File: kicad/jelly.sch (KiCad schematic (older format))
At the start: 41 parts, among them M1 PAGER_MOTOR, M2 PAGER_MOTOR, P1 CONN_01X01, P10 CONN_01X01, P11 CONN_01X01, P12 CONN_01X01, P13 CONN_01X01, P14 CONN_01X01, P15 CONN_01X01, P2 CONN_01X01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

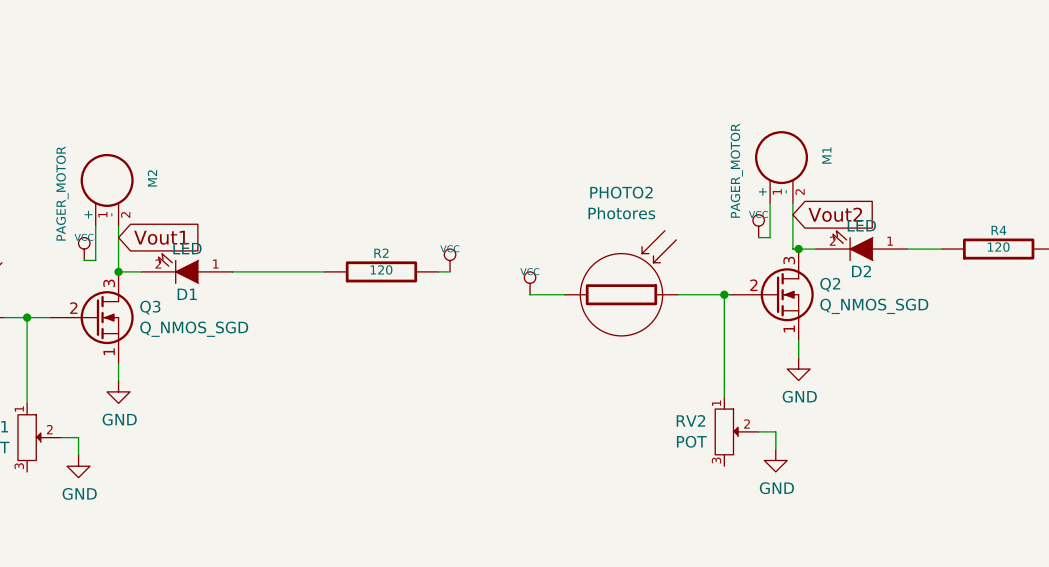
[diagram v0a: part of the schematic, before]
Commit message: Rename leds from D to LED
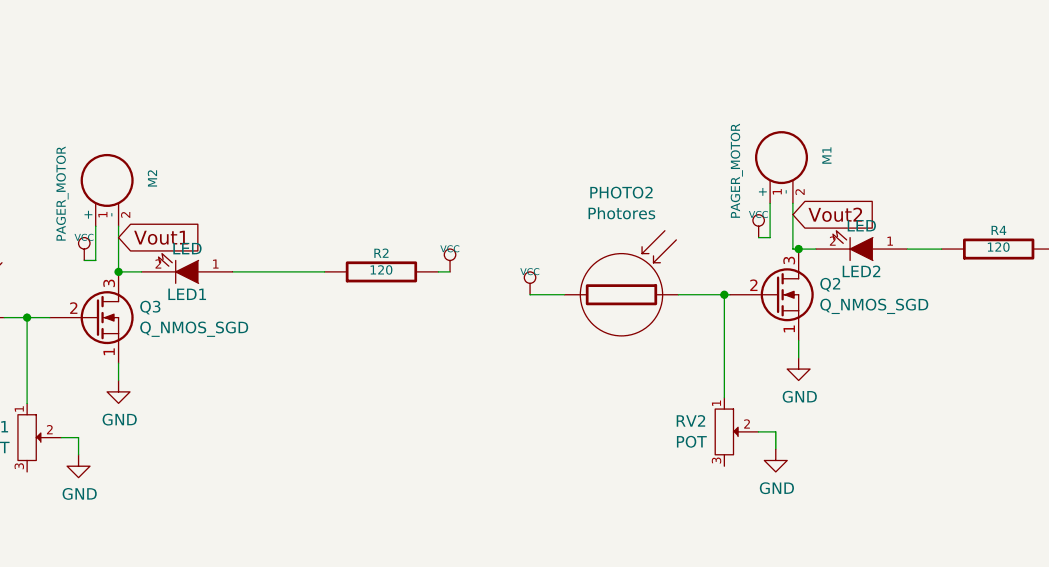
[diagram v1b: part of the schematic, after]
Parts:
- renumbered D1 to LED1, D2 to LED2
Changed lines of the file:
@@
 $EndComp
 $Comp
-L LED-RESCUE-bristle_bot D2
+L LED-RESCUE-bristle_bot LED2
 U 1 1 57C0D39F
 P 8600 2600
-F 0 "D2" H 8600 2700 50  0000 C CNN
+F 0 "LED2" H 8600 2700 50  0000 C CNN
 F 1 "LED" H 8600 2500 50  0000 C CNN
 F 2 "KiCad/LEDs.pretty:LED-5MM" H 8600 2600 29  0001 C CNN
@@
 $EndComp
 $Comp
-L LED-RESCUE-bristle_bot D1
+L LED-RESCUE-bristle_bot LED1
 U 1 1 57C0D3A3
 P 5650 2700
-F 0 "D1" H 5650 2800 50  0000 C CNN
+F 0 "LED1" H 5650 2800 50  0000 C CNN
 F 1 "LED" H 5650 2600 50  0000 C CNN
 F 2 "KiCad/LEDs.pretty:LED-5MM" H 5650 2700 60  0001 C CNN

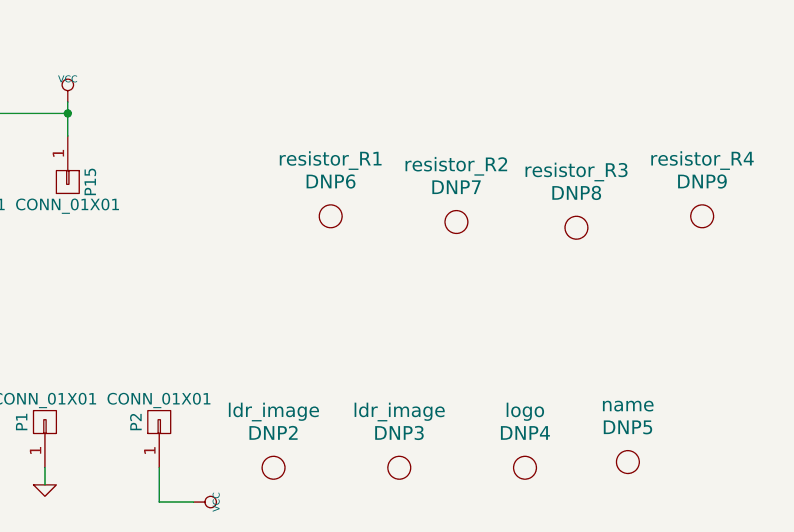
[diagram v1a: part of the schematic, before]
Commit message: Add page motor silkscreen image
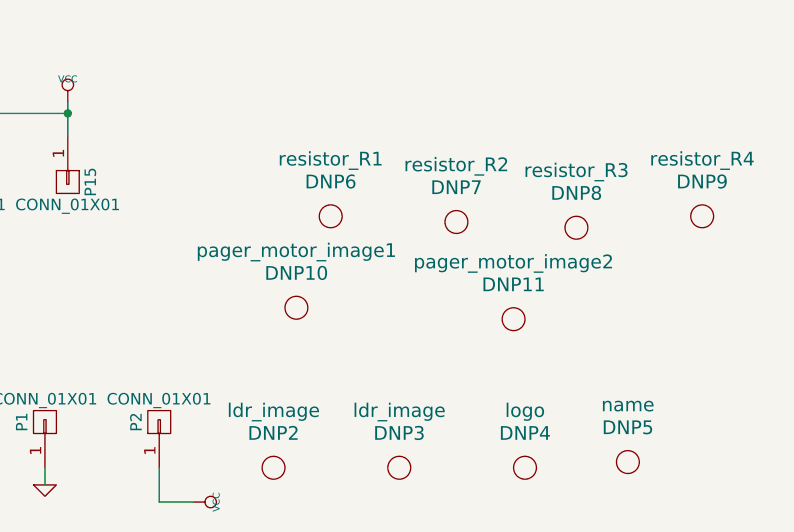
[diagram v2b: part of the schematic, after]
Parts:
- added DNP10: pager_motor_image1, custom:page_motor_image, symbol placeholder
- added DNP11: pager_motor_image2, custom:page_motor_image_flipped, symbol placeholder
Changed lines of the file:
@@
+	1    0    0    -1
+$EndComp
+$Comp
+L placeholder DNP10
+U 1 1 5802A5F3
+P 8900 5500
+F 0 "DNP10" H 8900 5650 60  0000 C CNN
+F 1 "pager_motor_image1" H 8900 5750 60  0000 C CNN
+F 2 "custom:page_motor_image" H 8900 5650 60  0001 C CNN
+F 3 "" H 8900 5650 60  0001 C CNN
+	1    8900 5500
+	1    0    0    -1
+$EndComp
+$Comp
+L placeholder DNP11
+U 1 1 5802A756
+P 9850 5550
+F 0 "DNP11" H 9850 5700 60  0000 C CNN
+F 1 "pager_motor_image2" H 9850 5800 60  0000 C CNN
+F 2 "custom:page_motor_image_flipped" H 9850 5700 60  0001 C CNN
+F 3 "" H 9850 5700 60  0001 C CNN
+	1    9850 5550
 	1    0    0    -1
 $EndComp

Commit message: Add plus and minus labels
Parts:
- added DNP12: plus1, custom:plus, symbol placeholder
- added DNP13: minus1, custom:minus, symbol placeholder
- BT1, SW1: footprint KiCad/Pin_Headers.pretty:Pin_Header_Straight_1x02 -> custom:Pin_Header_Straight_1x02
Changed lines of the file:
@@
 F 0 "BT1" H 1325 1925 50  0000 C CNN
 F 1 "BATTERY" H 1325 1535 50  0000 C CNN
-F 2 "KiCad/Pin_Headers.pretty:Pin_Header_Straight_1x02" H 1325 1725 29  0001 C CNN
+F 2 "custom:Pin_Header_Straight_1x02" H 1325 1725 29  0001 C CNN
 F 3 "~" H 1325 1725 60  0000 C CNN
 	1    1325 1725
@@
 F 0 "SW1" V 2271 1922 50  0000 R CNN
 F 1 "SPST" V 2180 1922 50  0000 R CNN
-F 2 "KiCad/Pin_Headers.pretty:Pin_Header_Straight_1x02" H 2225 2000 50  0001 C CNN
+F 2 "custom:Pin_Header_Straight_1x02" H 2225 2000 50  0001 C CNN
 F 3 "" H 2225 2000 50  0000 C CNN
 	1    2225 2000
@@
 	1    0    0    -1
 $EndComp
+$Comp
+L placeholder DNP12
+U 1 1 5802B04C
+P 10600 5625
+F 0 "DNP12" H 10600 5775 60  0000 C CNN
+F 1 "plus1" H 10600 5875 60  0000 C CNN
+F 2 "custom:plus" H 10600 5775 60  0001 C CNN
+F 3 "" H 10600 5775 60  0001 C CNN
+	1    10600 5625
+	1    0    0    -1
+$EndComp
+$Comp
+L placeholder DNP13
+U 1 1 5802B75C
+P 10900 5700
+F 0 "DNP13" H 10900 5850 60  0000 C CNN
+F 1 "minus1" H 10900 5950 60  0000 C CNN
+F 2 "custom:minus" H 10900 5850 60  0001 C CNN
+F 3 "" H 10900 5850 60  0001 C CNN
+	1    10900 5700
+	1    0    0    -1
+$EndComp

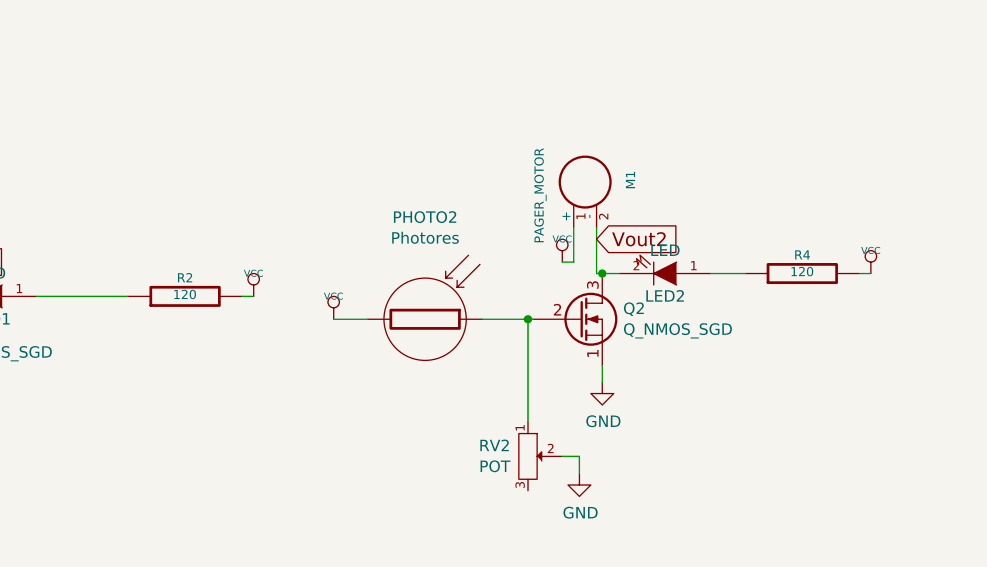
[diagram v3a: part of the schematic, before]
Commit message: Delete traces and make things more symmetrical
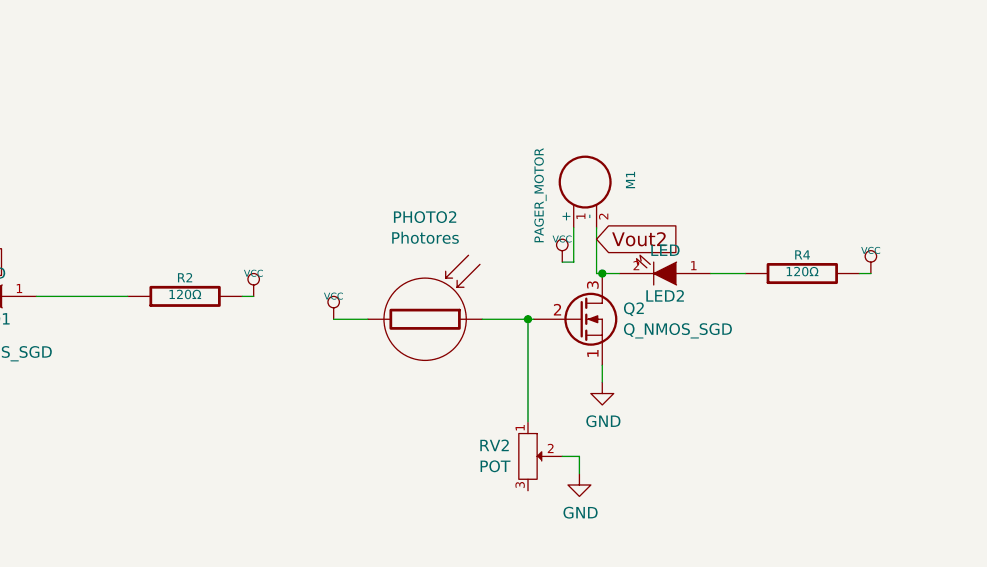
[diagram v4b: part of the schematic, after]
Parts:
- R2, R4: value 120 -> 120Ω
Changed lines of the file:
@@
 P 9200 2600
 F 0 "R4" V 9280 2600 40  0000 C CNN
-F 1 "120" V 9207 2601 40  0000 C CNN
+F 1 "120Ω" V 9207 2601 40  0000 C CNN
 F 2 "custom:R3-5" V 9130 2600 30  0001 C CNN
 F 3 "~" H 9200 2600 30  0000 C CNN
@@
 P 6500 2700
 F 0 "R2" V 6580 2700 40  0000 C CNN
-F 1 "120" V 6507 2701 40  0000 C CNN
+F 1 "120Ω" V 6507 2701 40  0000 C CNN
 F 2 "custom:R3-5" V 6430 2700 30  0001 C CNN
 F 3 "~" H 6500 2700 30  0000 C CNN

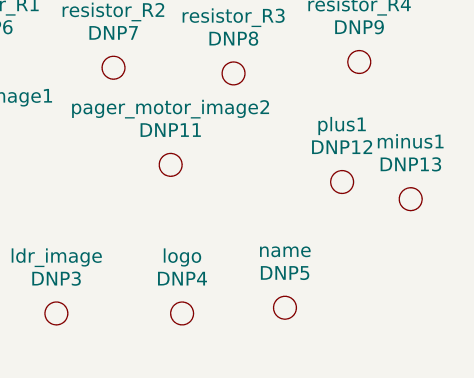
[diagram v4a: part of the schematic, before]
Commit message: Add mercury switch drawing
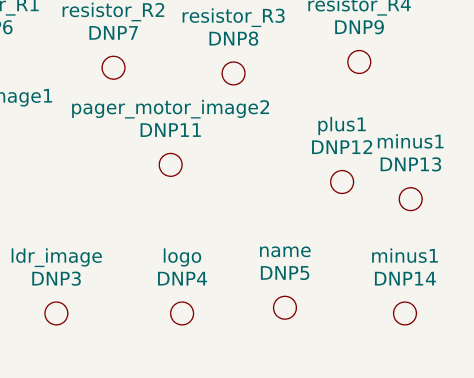
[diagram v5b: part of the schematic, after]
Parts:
- added DNP14: minus1, custom:mercury_switch, symbol placeholder
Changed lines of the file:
@@
 $EndComp
 $Comp
-L GND-RESCUE-bristle_bot #PWR01
+L GND-RESCUE-bristle_bot #PWR2
 U 1 1 57C0D38E
 P 1325 3225
-F 0 "#PWR01" H 1325 3225 30  0001 C CNN
+F 0 "#PWR2" H 1325 3225 30  0001 C CNN
 F 1 "GND" H 1325 3155 30  0001 C CNN
 F 2 "" H 1325 3225 60  0000 C CNN
@@
 $EndComp
 $Comp
-L VCC #PWR02
+L VCC #PWR1
 U 1 1 57C0D391
 P 1325 1275
-F 0 "#PWR02" H 1325 1375 30  0001 C CNN
+F 0 "#PWR1" H 1325 1375 30  0001 C CNN
 F 1 "VCC" H 1325 1375 30  0000 C CNN
 F 2 "" H 1325 1275 60  0001 C CNN
@@
 $EndComp
 $Comp
-L VCC #PWR03
+L VCC #PWR5
 U 1 1 57C0D393
 P 4200 2900
-F 0 "#PWR03" H 4200 3000 30  0001 C CNN
+F 0 "#PWR5" H 4200 3000 30  0001 C CNN
 F 1 "VCC" H 4200 3000 30  0000 C CNN
 F 2 "" H 4200 2900 60  0001 C CNN
@@
 $EndComp
 $Comp
-L VCC #PWR04
+L VCC #PWR8
 U 1 1 57C0D394
 P 5200 2650
-F 0 "#PWR04" H 5200 2750 30  0001 C CNN
+F 0 "#PWR8" H 5200 2750 30  0001 C CNN
 F 1 "VCC" H 5200 2750 30  0000 C CNN
 F 2 "" H 5200 2650 60  0001 C CNN
@@
 $EndComp
 $Comp
-L VCC #PWR05
+L VCC #PWR14
 U 1 1 57C0D397
 P 8150 2550
-F 0 "#PWR05" H 8150 2650 30  0001 C CNN
+F 0 "#PWR14" H 8150 2650 30  0001 C CNN
 F 1 "VCC" H 8150 2650 30  0000 C CNN
 F 2 "" H 8150 2550 60  0001 C CNN
@@
 $EndComp
 $Comp
-L VCC #PWR06
+L VCC #PWR11
 U 1 1 57C0D39B
 P 7150 2800
-F 0 "#PWR06" H 7150 2900 30  0001 C CNN
+F 0 "#PWR11" H 7150 2900 30  0001 C CNN
 F 1 "VCC" H 7150 2900 30  0000 C CNN
 F 2 "" H 7150 2800 60  0001 C CNN
@@
 $EndComp
 $Comp
-L VCC #PWR07
+L VCC #PWR18
 U 1 1 57C0D3A1
 P 9500 2600
-F 0 "#PWR07" H 9500 2700 30  0001 C CNN
+F 0 "#PWR18" H 9500 2700 30  0001 C CNN
 F 1 "VCC" H 9500 2700 30  0000 C CNN
 F 2 "" H 9500 2600 60  0001 C CNN
@@
 $EndComp
 $Comp
-L VCC #PWR08
+L VCC #PWR10
 U 1 1 57C0D3A4
 P 6800 2700
-F 0 "#PWR08" H 6800 2800 30  0001 C CNN
+F 0 "#PWR10" H 6800 2800 30  0001 C CNN
 F 1 "VCC" H 6800 2800 30  0000 C CNN
 F 2 "" H 6800 2700 60  0001 C CNN
@@
 $EndComp
 $Comp
-L VCC #PWR09
+L VCC #PWR3
 U 1 1 57C0D3B0
 P 1450 4350
-F 0 "#PWR09" H 1450 4450 30  0001 C CNN
+F 0 "#PWR3" H 1450 4450 30  0001 C CNN
 F 1 "VCC" H 1450 4450 30  0000 C CNN
 F 2 "" H 1450 4350 60  0001 C CNN
@@
 $EndComp
 $Comp
-L VCC #PWR010
+L VCC #PWR13
 U 1 1 57C309E3
 P 7900 4600
-F 0 "#PWR010" H 7900 4700 30  0001 C CNN
+F 0 "#PWR13" H 7900 4700 30  0001 C CNN
 F 1 "VCC" H 7900 4700 30  0000 C CNN
 F 2 "" H 7900 4600 60  0001 C CNN
@@
 Vout2
 $Comp
-L GND-RESCUE-bristle_bot #PWR011
+L GND-RESCUE-bristle_bot #PWR6
 U 1 1 57C36163
 P 4600 4550
-F 0 "#PWR011" H 4600 4550 30  0001 C CNN
+F 0 "#PWR6" H 4600 4550 30  0001 C CNN
 F 1 "GND" H 4600 4480 30  0001 C CNN
 F 2 "" H 4600 4550 60  0001 C CNN
@@
 $EndComp
 $Comp
-L VCC #PWR012
+L VCC #PWR17
 U 1 1 57C3486C
 P 8450 6350
-F 0 "#PWR012" H 8450 6450 30  0001 C CNN
+F 0 "#PWR17" H 8450 6450 30  0001 C CNN
 F 1 "VCC" H 8450 6450 30  0000 C CNN
 F 2 "" H 8450 6350 60  0001 C CNN
@@
 $EndComp
 $Comp
-L GND #PWR013
+L GND #PWR9
 U 1 1 57EC11E5
 P 5350 3175
-F 0 "#PWR013" H 5350 2925 50  0001 C CNN
+F 0 "#PWR9" H 5350 2925 50  0001 C CNN
 F 1 "GND" H 5355 3002 50  0000 C CNN
 F 2 "" H 5350 3175 50  0000 C CNN
@@
 $EndComp
 $Comp
-L GND #PWR014
+L GND #PWR16
 U 1 1 57EC1326
 P 8325 3075
-F 0 "#PWR014" H 8325 2825 50  0001 C CNN
+F 0 "#PWR16" H 8325 2825 50  0001 C CNN
 F 1 "GND" H 8330 2902 50  0000 C CNN
 F 2 "" H 8325 3075 50  0000 C CNN
@@
 $EndComp
 $Comp
-L GND #PWR015
+L GND #PWR7
 U 1 1 57EC1A42
 P 5175 3500
-F 0 "#PWR015" H 5175 3250 50  0001 C CNN
+F 0 "#PWR7" H 5175 3250 50  0001 C CNN
 F 1 "GND" H 5180 3327 50  0000 C CNN
 F 2 "" H 5175 3500 50  0000 C CNN
@@
 $EndComp
 $Comp
-L GND #PWR016
+L GND #PWR15
 U 1 1 57EC1E47
 P 8225 3475
-F 0 "#PWR016" H 8225 3225 50  0001 C CNN
+F 0 "#PWR15" H 8225 3225 50  0001 C CNN
 F 1 "GND" H 8230 3302 50  0000 C CNN
 F 2 "" H 8225 3475 50  0000 C CNN
@@
 Connection ~ 2225 3000
 $Comp
-L GND-RESCUE-bristle_bot #PWR017
+L GND-RESCUE-bristle_bot #PWR4
 U 1 1 57EC6243
 P 2225 3575
-F 0 "#PWR017" H 2225 3575 30  0001 C CNN
+F 0 "#PWR4" H 2225 3575 30  0001 C CNN
 F 1 "GND" H 2225 3505 30  0001 C CNN
 F 2 "" H 2225 3575 60  0000 C CNN
@@
 	1325 2700 1325 2025
 $Comp
-L GND-RESCUE-bristle_bot #PWR018
+L GND-RESCUE-bristle_bot #PWR12
 U 1 1 57F92FC8
 P 7800 6275
-F 0 "#PWR018" H 7800 6275 30  0001 C CNN
+F 0 "#PWR12" H 7800 6275 30  0001 C CNN
 F 1 "GND" H 7800 6205 30  0001 C CNN
 F 2 "" H 7800 6275 60  0000 C CNN
@@
 	1    0    0    -1
 $EndComp
+$Comp
+L placeholder DNP14
+U 1 1 5802C4A0
+P 10875 6200
+F 0 "DNP14" H 10875 6350 60  0000 C CNN
+F 1 "minus1" H 10875 6450 60  0000 C CNN
+F 2 "custom:mercury_switch" H 10875 6350 60  0001 C CNN
+F 3 "" H 10875 6350 60  0001 C CNN
+	1    10875 6200
+	1    0    0    -1
+$EndComp

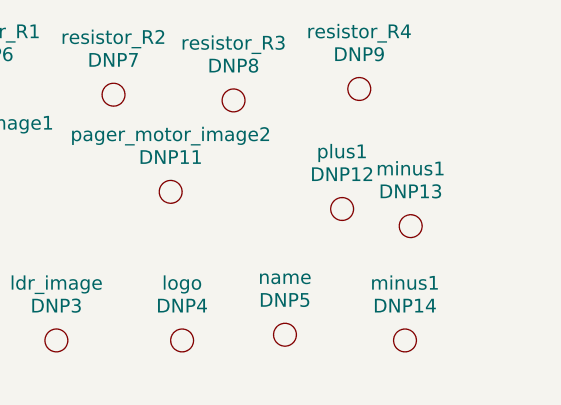
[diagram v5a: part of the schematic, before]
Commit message: Make sure footprints and schematic are in sync
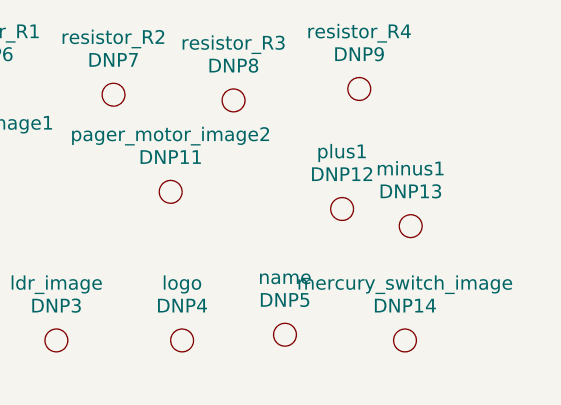
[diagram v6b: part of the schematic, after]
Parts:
- DNP14: value minus1 -> mercury_switch_image
- SW1: footprint custom:Pin_Header_Straight_1x02 -> custom:MERCURY_SWITCH_HEADER
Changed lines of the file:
@@
 $EndComp
 $Comp
-L GND-RESCUE-bristle_bot #PWR2
+L GND-RESCUE-bristle_bot #PWR01
 U 1 1 57C0D38E
 P 1325 3225
-F 0 "#PWR2" H 1325 3225 30  0001 C CNN
+F 0 "#PWR01" H 1325 3225 30  0001 C CNN
 F 1 "GND" H 1325 3155 30  0001 C CNN
 F 2 "" H 1325 3225 60  0000 C CNN
@@
 $EndComp
 $Comp
-L VCC #PWR1
+L VCC #PWR02
 U 1 1 57C0D391
 P 1325 1275
-F 0 "#PWR1" H 1325 1375 30  0001 C CNN
+F 0 "#PWR02" H 1325 1375 30  0001 C CNN
 F 1 "VCC" H 1325 1375 30  0000 C CNN
 F 2 "" H 1325 1275 60  0001 C CNN
@@
 $EndComp
 $Comp
-L VCC #PWR5
+L VCC #PWR03
 U 1 1 57C0D393
 P 4200 2900
-F 0 "#PWR5" H 4200 3000 30  0001 C CNN
+F 0 "#PWR03" H 4200 3000 30  0001 C CNN
 F 1 "VCC" H 4200 3000 30  0000 C CNN
 F 2 "" H 4200 2900 60  0001 C CNN
@@
 $EndComp
 $Comp
-L VCC #PWR8
+L VCC #PWR04
 U 1 1 57C0D394
 P 5200 2650
-F 0 "#PWR8" H 5200 2750 30  0001 C CNN
+F 0 "#PWR04" H 5200 2750 30  0001 C CNN
 F 1 "VCC" H 5200 2750 30  0000 C CNN
 F 2 "" H 5200 2650 60  0001 C CNN
@@
 $EndComp
 $Comp
-L VCC #PWR14
+L VCC #PWR05
 U 1 1 57C0D397
 P 8150 2550
-F 0 "#PWR14" H 8150 2650 30  0001 C CNN
+F 0 "#PWR05" H 8150 2650 30  0001 C CNN
 F 1 "VCC" H 8150 2650 30  0000 C CNN
 F 2 "" H 8150 2550 60  0001 C CNN
@@
 $EndComp
 $Comp
-L VCC #PWR11
+L VCC #PWR06
 U 1 1 57C0D39B
 P 7150 2800
-F 0 "#PWR11" H 7150 2900 30  0001 C CNN
+F 0 "#PWR06" H 7150 2900 30  0001 C CNN
 F 1 "VCC" H 7150 2900 30  0000 C CNN
 F 2 "" H 7150 2800 60  0001 C CNN
@@
 $EndComp
 $Comp
-L VCC #PWR18
+L VCC #PWR07
 U 1 1 57C0D3A1
 P 9500 2600
-F 0 "#PWR18" H 9500 2700 30  0001 C CNN
+F 0 "#PWR07" H 9500 2700 30  0001 C CNN
 F 1 "VCC" H 9500 2700 30  0000 C CNN
 F 2 "" H 9500 2600 60  0001 C CNN
@@
 $EndComp
 $Comp
-L VCC #PWR10
+L VCC #PWR08
 U 1 1 57C0D3A4
 P 6800 2700
-F 0 "#PWR10" H 6800 2800 30  0001 C CNN
+F 0 "#PWR08" H 6800 2800 30  0001 C CNN
 F 1 "VCC" H 6800 2800 30  0000 C CNN
 F 2 "" H 6800 2700 60  0001 C CNN
@@
 $EndComp
 $Comp
-L VCC #PWR3
+L VCC #PWR09
 U 1 1 57C0D3B0
 P 1450 4350
-F 0 "#PWR3" H 1450 4450 30  0001 C CNN
+F 0 "#PWR09" H 1450 4450 30  0001 C CNN
 F 1 "VCC" H 1450 4450 30  0000 C CNN
 F 2 "" H 1450 4350 60  0001 C CNN
@@
 $EndComp
 $Comp
-L VCC #PWR13
+L VCC #PWR010
 U 1 1 57C309E3
 P 7900 4600
-F 0 "#PWR13" H 7900 4700 30  0001 C CNN
+F 0 "#PWR010" H 7900 4700 30  0001 C CNN
 F 1 "VCC" H 7900 4700 30  0000 C CNN
 F 2 "" H 7900 4600 60  0001 C CNN
@@
 Vout2
 $Comp
-L GND-RESCUE-bristle_bot #PWR6
+L GND-RESCUE-bristle_bot #PWR011
 U 1 1 57C36163
 P 4600 4550
-F 0 "#PWR6" H 4600 4550 30  0001 C CNN
+F 0 "#PWR011" H 4600 4550 30  0001 C CNN
 F 1 "GND" H 4600 4480 30  0001 C CNN
 F 2 "" H 4600 4550 60  0001 C CNN
@@
 $EndComp
 $Comp
-L VCC #PWR17
+L VCC #PWR012
 U 1 1 57C3486C
 P 8450 6350
-F 0 "#PWR17" H 8450 6450 30  0001 C CNN
+F 0 "#PWR012" H 8450 6450 30  0001 C CNN
 F 1 "VCC" H 8450 6450 30  0000 C CNN
 F 2 "" H 8450 6350 60  0001 C CNN
@@
 $EndComp
 $Comp
-L GND #PWR9
+L GND #PWR013
 U 1 1 57EC11E5
 P 5350 3175
-F 0 "#PWR9" H 5350 2925 50  0001 C CNN
+F 0 "#PWR013" H 5350 2925 50  0001 C CNN
 F 1 "GND" H 5355 3002 50  0000 C CNN
 F 2 "" H 5350 3175 50  0000 C CNN
@@
 $EndComp
 $Comp
-L GND #PWR16
+L GND #PWR014
 U 1 1 57EC1326
 P 8325 3075
-F 0 "#PWR16" H 8325 2825 50  0001 C CNN
+F 0 "#PWR014" H 8325 2825 50  0001 C CNN
 F 1 "GND" H 8330 2902 50  0000 C CNN
 F 2 "" H 8325 3075 50  0000 C CNN
@@
 $EndComp
 $Comp
-L GND #PWR7
+L GND #PWR015
 U 1 1 57EC1A42
 P 5175 3500
-F 0 "#PWR7" H 5175 3250 50  0001 C CNN
+F 0 "#PWR015" H 5175 3250 50  0001 C CNN
 F 1 "GND" H 5180 3327 50  0000 C CNN
 F 2 "" H 5175 3500 50  0000 C CNN
@@
 $EndComp
 $Comp
-L GND #PWR15
+L GND #PWR016
 U 1 1 57EC1E47
 P 8225 3475
-F 0 "#PWR15" H 8225 3225 50  0001 C CNN
+F 0 "#PWR016" H 8225 3225 50  0001 C CNN
 F 1 "GND" H 8230 3302 50  0000 C CNN
 F 2 "" H 8225 3475 50  0000 C CNN
@@
 Connection ~ 2225 3000
 $Comp
-L GND-RESCUE-bristle_bot #PWR4
+L GND-RESCUE-bristle_bot #PWR017
 U 1 1 57EC6243
 P 2225 3575
-F 0 "#PWR4" H 2225 3575 30  0001 C CNN
+F 0 "#PWR017" H 2225 3575 30  0001 C CNN
 F 1 "GND" H 2225 3505 30  0001 C CNN
 F 2 "" H 2225 3575 60  0000 C CNN
@@
 F 0 "SW1" V 2271 1922 50  0000 R CNN
 F 1 "SPST" V 2180 1922 50  0000 R CNN
-F 2 "custom:Pin_Header_Straight_1x02" H 2225 2000 50  0001 C CNN
+F 2 "custom:MERCURY_SWITCH_HEADER" H 2225 2000 50  0001 C CNN
 F 3 "" H 2225 2000 50  0000 C CNN
 	1    2225 2000
@@
 	1325 2700 1325 2025
 $Comp
-L GND-RESCUE-bristle_bot #PWR12
+L GND-RESCUE-bristle_bot #PWR018
 U 1 1 57F92FC8
 P 7800 6275
-F 0 "#PWR12" H 7800 6275 30  0001 C CNN
+F 0 "#PWR018" H 7800 6275 30  0001 C CNN
 F 1 "GND" H 7800 6205 30  0001 C CNN
 F 2 "" H 7800 6275 60  0000 C CNN
@@
 P 10875 6200
 F 0 "DNP14" H 10875 6350 60  0000 C CNN
-F 1 "minus1" H 10875 6450 60  0000 C CNN
+F 1 "mercury_switch_image" H 10875 6450 60  0000 C CNN
 F 2 "custom:mercury_switch" H 10875 6350 60  0001 C CNN
 F 3 "" H 10875 6350 60  0001 C CNN
